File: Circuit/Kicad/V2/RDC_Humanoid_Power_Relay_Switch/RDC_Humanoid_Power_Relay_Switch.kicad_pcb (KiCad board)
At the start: 2 copper layers, 12 parts, among them J1 XT60, J2 VH, J3 XA, Q1 TK7R4A10RL

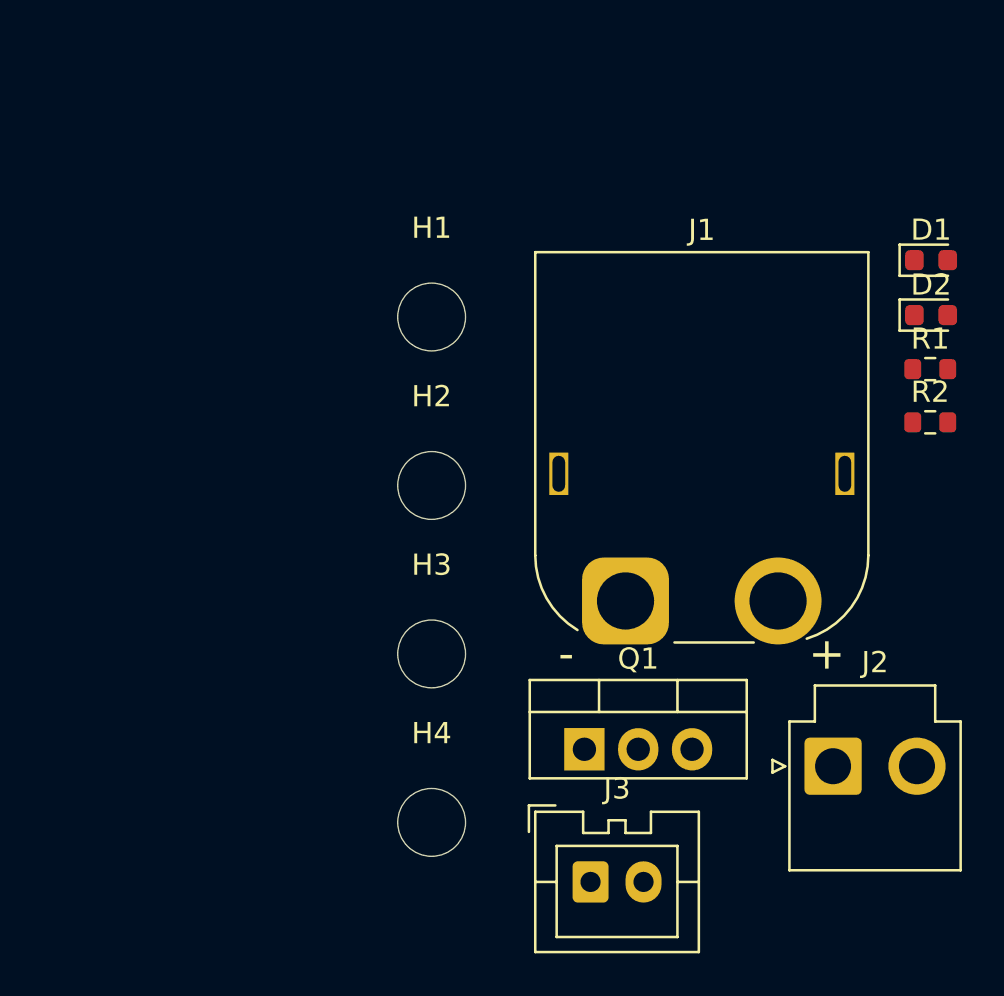
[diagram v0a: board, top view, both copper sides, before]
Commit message: Relay_Switchの回路図とPCBを組んでみた。
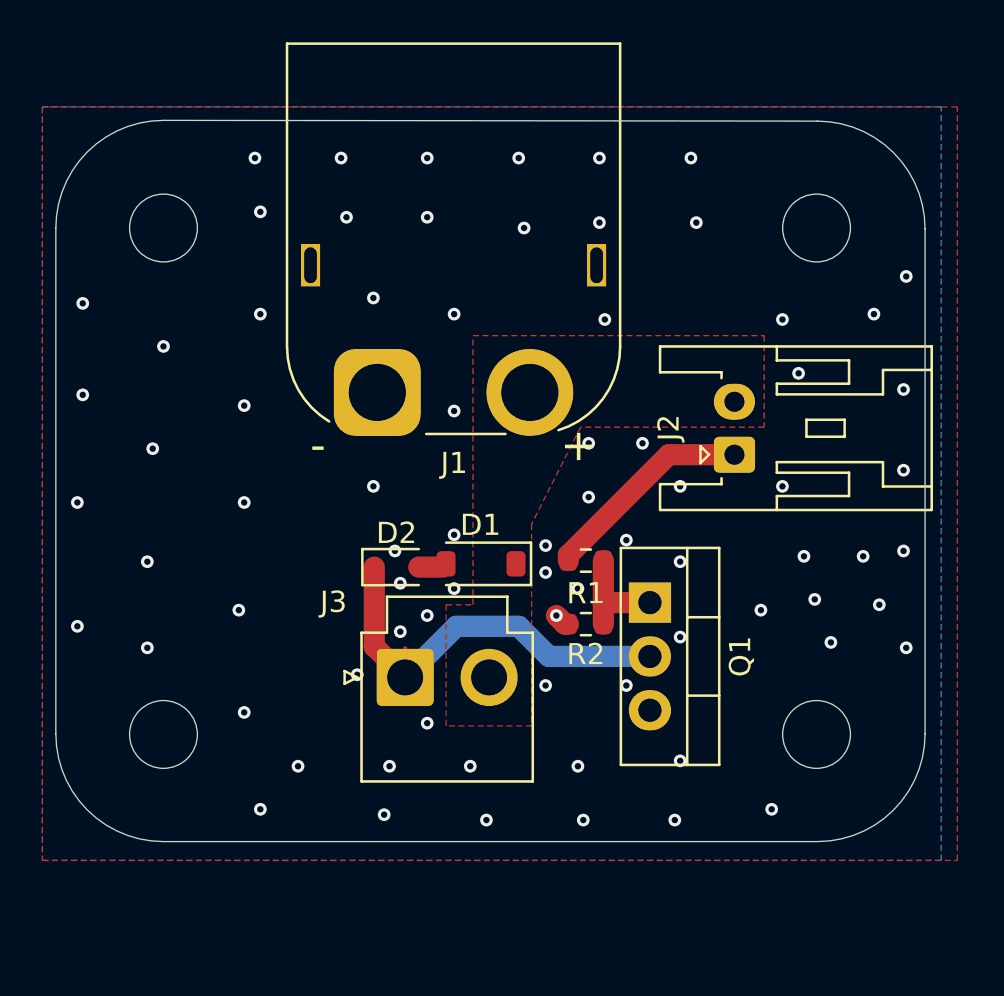
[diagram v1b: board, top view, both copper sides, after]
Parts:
- D1: footprint Diode_SMD:D_0603_1608Metric -> Diode_SMD:D_SOD-123
- D2: footprint Diode_SMD:D_0603_1608Metric -> Diode_SMD:D_SOD-323
- J2: value VH -> XA; footprint Connector_JST:JST_VH_B2P-VH_1x02_P3.96mm_Vertical -> Connector_JST:JST_XA_S02B-XASK-1_1x02_P2.50mm_Horizontal
- J3: value XA -> VH; footprint Connector_JST:JST_XA_B02B-XASK-1_1x02_P2.50mm_Vertical -> Connector_JST:JST_VH_B2P-VH_1x02_P3.96mm_Vertical
- R1: value R_5k -> R_10k
- moved D2 27.9 mm to (54.2, 54.1)
- moved H3 27.1 mm to (74.0, 38.1)
- moved D1 25.6 mm to (58.2, 53.9), turned to 180 degrees
- moved R2 18.8 mm to (63.1, 56.8), turned to 180 degrees
- moved H4 18.6 mm to (74.0, 62.0)
- moved R1 18.6 mm to (63.1, 53.8)
- moved H2 17.3 mm to (43.2, 62.0)
- moved J2 15.4 mm to (70.1, 48.8), turned to 90 degrees
- moved J1 15.3 mm to (53.3, 45.9)
- moved H1 13.3 mm to (43.2, 38.1)
- moved J3 13.0 mm to (54.6, 59.3)
- moved Q1 7.58 mm to (66.1, 55.8), turned to -90 degrees
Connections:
- J1 pad 1: +12V -> GND
- J1 pad 2: GND -> +12V
- J2 pad 1: +12V -> Net-(J2-Pin_1)
- J2 pad 2: Net-(J2-Pin_2) -> +12V
- J3 pad 1: +12V -> Net-(D2-K)
- J3 pad 2: Net-(D2-K) -> +12V
- R1 pad 1: Net-(J2-Pin_2) -> Net-(J2-Pin_1)
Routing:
- net Net-(D2-K): track 0.00 -> 20.3 mm
- net Net-(J2-Pin_1): track 0.00 -> 10.1 mm
- net Net-(Q1-G): track 0.00 -> 5.24 mm
- net Net-(D1-A): track 0.00 -> 1.35 mm
- net GND: track 0.00 -> 0.74 mm, vias 0 -> 77
- added copper zone on F.Cu, net +12V
- added copper zone on B.Cu, net GND
- added copper zone on F.Cu, net GND
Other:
- board outline added: 41 x 34 mm

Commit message: アドバイスを元に修正。Relay Switch用の基板ができた。
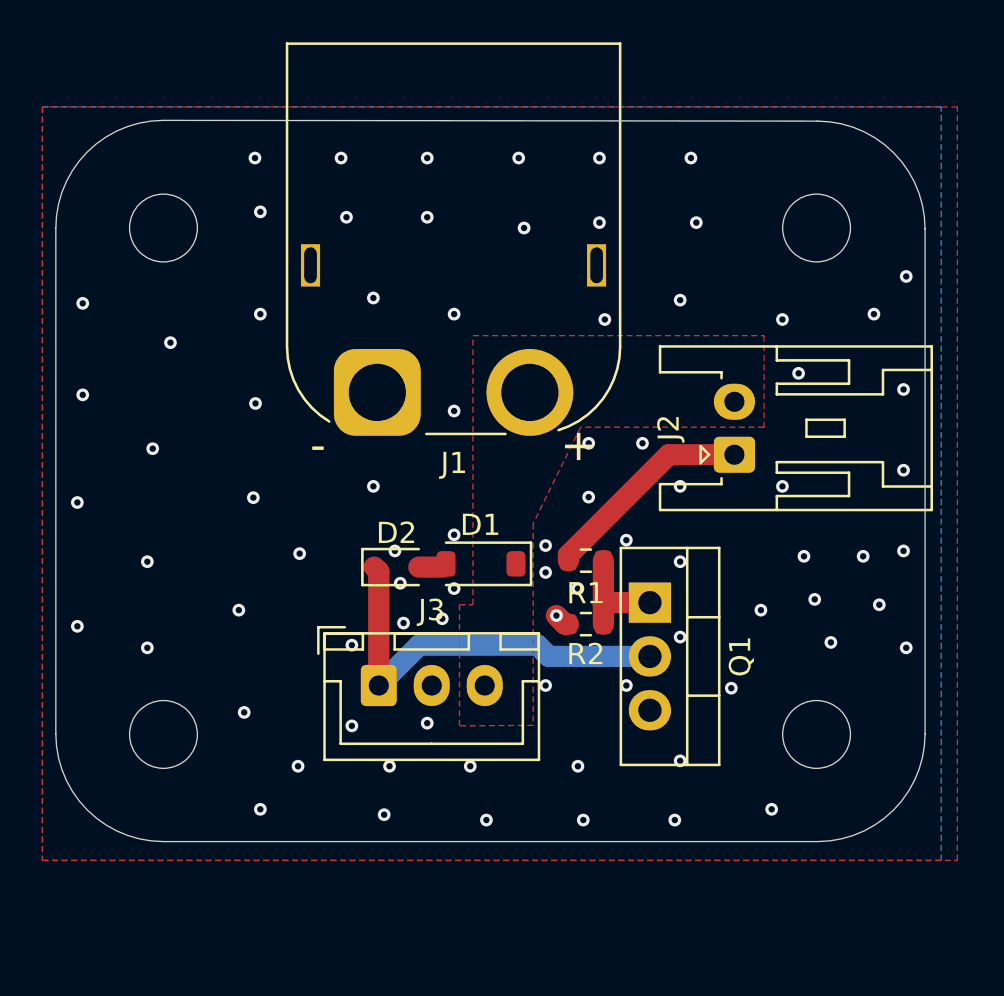
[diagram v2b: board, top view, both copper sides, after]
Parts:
- J3: footprint Connector_JST:JST_VH_B2P-VH_1x02_P3.96mm_Vertical -> Connector_JST:JST_XH_B3B-XH-A_1x03_P2.50mm_Vertical
- R1: value R_10k -> R_100
- moved J3 1.30 mm to (53.3, 59.7)
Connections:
- J3 pad 2: +12V -> unconnected-(J3-Pin_2-Pad2)
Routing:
- net Net-(D2-K): track 20.3 -> 19.5 mm
- net GND: vias 77 -> 81
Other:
- board text added: "RDC_Bipedal_Robot - Circuit Name : Relay_Switch - Version : 2.0 - Designed Date : 2025/03/25 - Designer Name - Yusuke Yamasaki - Yuya Mochizuki"
